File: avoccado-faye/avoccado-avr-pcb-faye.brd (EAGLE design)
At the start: 25 x 24.5 mm, 58 parts, among them Q1 16MHz, Q2 FET, U2 MCP73831

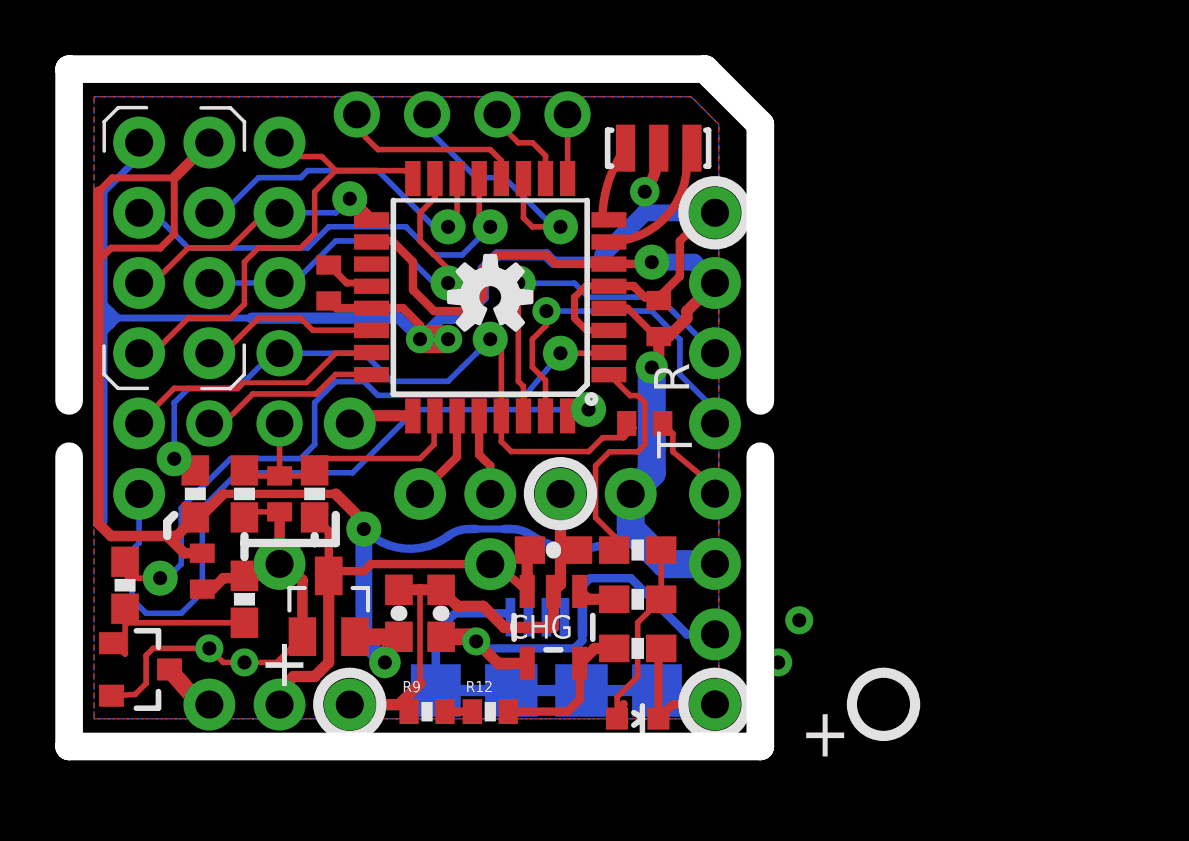
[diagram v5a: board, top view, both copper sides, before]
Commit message: add test points
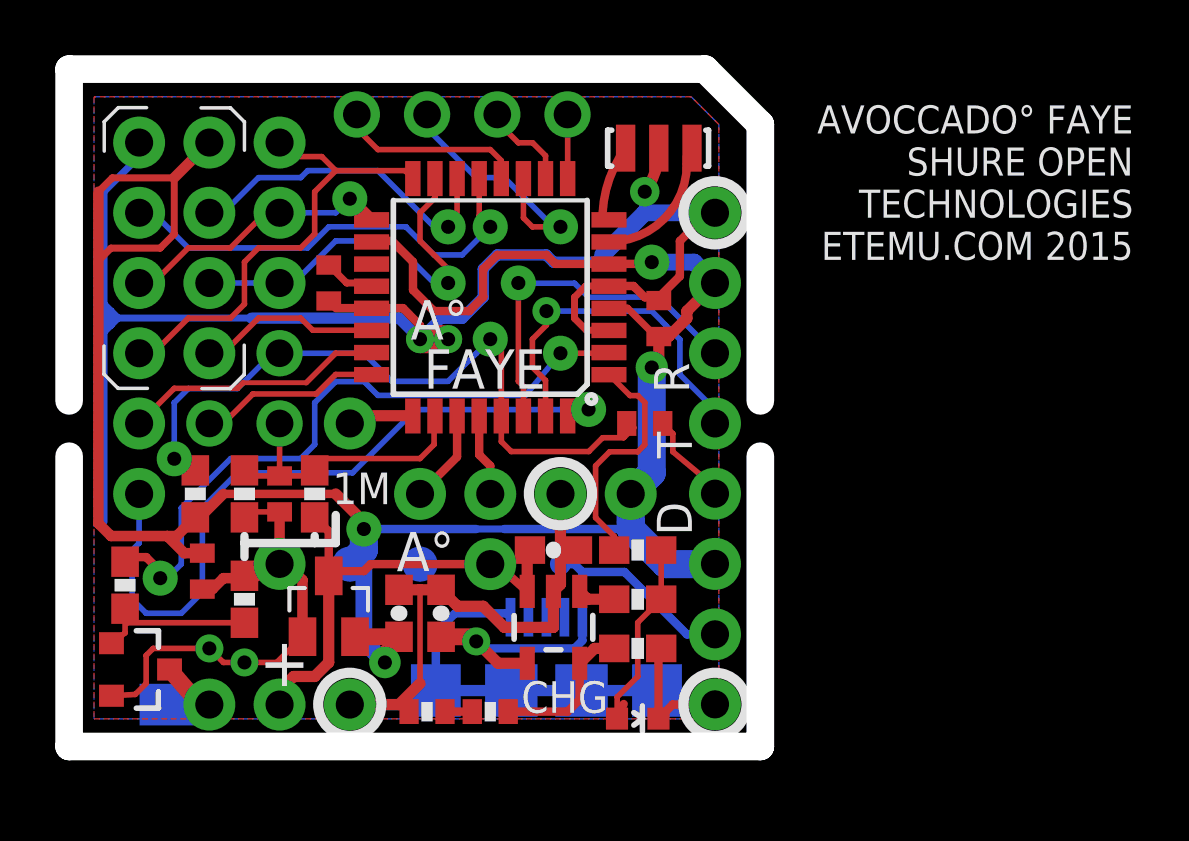
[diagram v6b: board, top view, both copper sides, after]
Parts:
- added JP16: M01SMD-4.5X1.5, SparkFun-Connectors:PAD-1.5X4.5
- added TP3, TP5: TEST-POINT3X5, SparkFun-Passives:PAD.03X.05
- added TP4: TEST-POINT3, SparkFun-Passives:PAD.03X.03
- moved LOGO2 8.27 mm to (20.8, 21.3), flipped to the bottom
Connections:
- net 3.3V: now also TP5.P$1
- net 5V: now also TP4.P$1
- net GND: now also TP3.P$1
- net VIBR: now also JP16.P$1
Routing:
- net VIBR: track 2.02 -> 3.55 mm
- net 3.3V: track 84.7 -> 86.2 mm
- net 5V: track 15.3 -> 16.7 mm
- net N$6: track 6.62 -> 5.85 mm
- net GND: vias 7 -> 5
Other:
- board text added: "1M"
- board text added: "4"
- board text added: "A°"
- board text added: "BAT"
- board text added: "D"
- board text added: "FAYE"
- board text added: "VB"
- board text added: "VC"
- board text removed: "D4"
- board text removed: "DT"
- board text removed: "RX"
- board text removed: "TX"
- board text removed: "Vb"
- board text removed: "Vc"
- board text removed: "Vin"

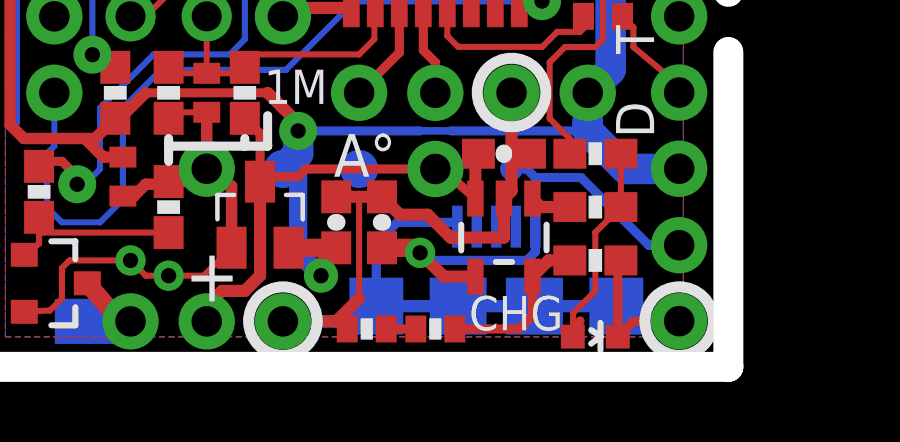
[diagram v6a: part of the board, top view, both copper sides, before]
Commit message: spread 0402 resistors
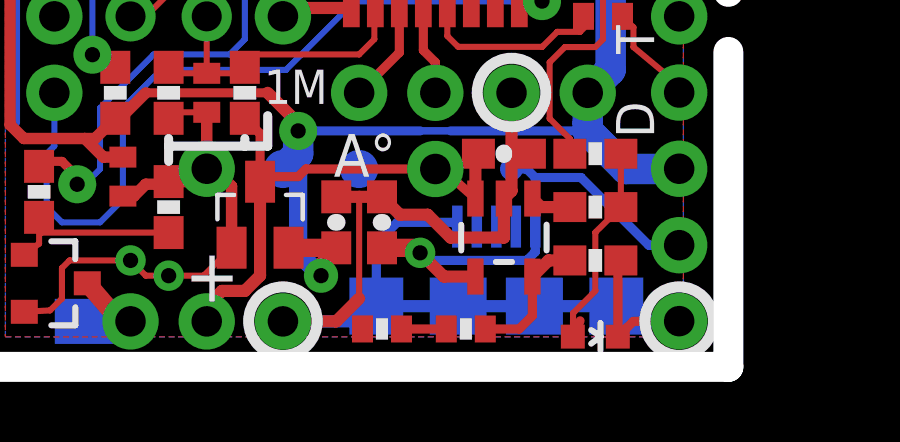
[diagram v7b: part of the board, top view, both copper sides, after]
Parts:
- moved R12 1.02 mm to (15.7, 0.76)
- moved R9 0.51 mm to (13.0, 0.76)
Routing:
- net CHG-PROG: track 5.55 -> 4.53 mm
- net N$3: track 0.99 -> 1.49 mm
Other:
- board text removed: "CHG"
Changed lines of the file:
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@@
 <text x="21.29" y="13.384" size="1.27" layer="21" ratio="15" rot="SR90" align="center-right">R</text>
 <rectangle x1="10.668" y1="11.684" x2="18.796" y2="19.812" layer="41"/>
-<text x="18.996" y="1.289" size="1.143" layer="21" font="vector" ratio="15" rot="R180" align="center-left">CHG</text>
 <circle x="17.272" y="8.644" radius="1.143" width="0.3683" layer="21"/>
 <circle x="22.86" y="1.024" radius="1.143" width="0.3683" layer="21"/>
@@
 <param name="dpMaxLengthDifference" value="10mm"/>
 <param name="dpGapFactor" value="2.5"/>
-<param name="checkGrid" value="1"/>
-<param name="checkAngle" value="1"/>
+<param name="checkGrid" value="0"/>
+<param name="checkAngle" value="0"/>
 <param name="checkFont" value="1"/>
 <param name="checkRestrict" value="0"/>
@@
 <attribute name="PROD_ID" value="CONN-09505" x="16.764" y="1.524" size="1.778" layer="28" font="vector" ratio="15" rot="MR0" display="off"/>
 </element>
-<element name="R12" library="SparkFun-Resistors" package="0402-RES" value="1K" x="14.732" y="0.762" smashed="yes">
-<attribute name="VALUE" x="14.4145" y="1.397" size="0.4064" layer="27"/>
+<element name="R12" library="SparkFun-Resistors" package="0402-RES" value="1K" x="15.748" y="0.762" smashed="yes">
+<attribute name="VALUE" x="15.4305" y="1.397" size="0.4064" layer="27"/>
 </element>
-<element name="R9" library="SparkFun-Resistors" package="0402-RES" value="1K" x="12.446" y="0.762" smashed="yes">
-<attribute name="VALUE" x="12.1285" y="1.397" size="0.4064" layer="27"/>
+<element name="R9" library="SparkFun-Resistors" package="0402-RES" value="1K" x="12.954" y="0.762" smashed="yes">
+<attribute name="VALUE" x="12.6365" y="1.397" size="0.4064" layer="27"/>
 </element>
 <element name="TP5" library="SparkFun-Passives" package="PAD.03X.05" value="TEST-POINT3X5" x="9.652" y="6.096" rot="MR0"/>
@@
 <wire x1="17.968" y1="2.5099" x2="17.968" y2="1.204" width="0.3048" layer="1"/>
 <wire x1="17.968" y1="1.204" x2="17.526" y2="0.762" width="0.3048" layer="1"/>
-<wire x1="17.526" y1="0.762" x2="15.382" y2="0.762" width="0.3048" layer="1"/>
+<wire x1="17.526" y1="0.762" x2="16.398" y2="0.762" width="0.3048" layer="1"/>
 </signal>
 <signal name="5V">
@@
 <contactref element="R12" pad="1"/>
 <contactref element="R9" pad="2"/>
-<wire x1="14.082" y1="0.762" x2="13.096" y2="0.762" width="0.3048" layer="1"/>
+<wire x1="15.098" y1="0.762" x2="13.604" y2="0.762" width="0.3048" layer="1"/>
 </signal>
 </signals>

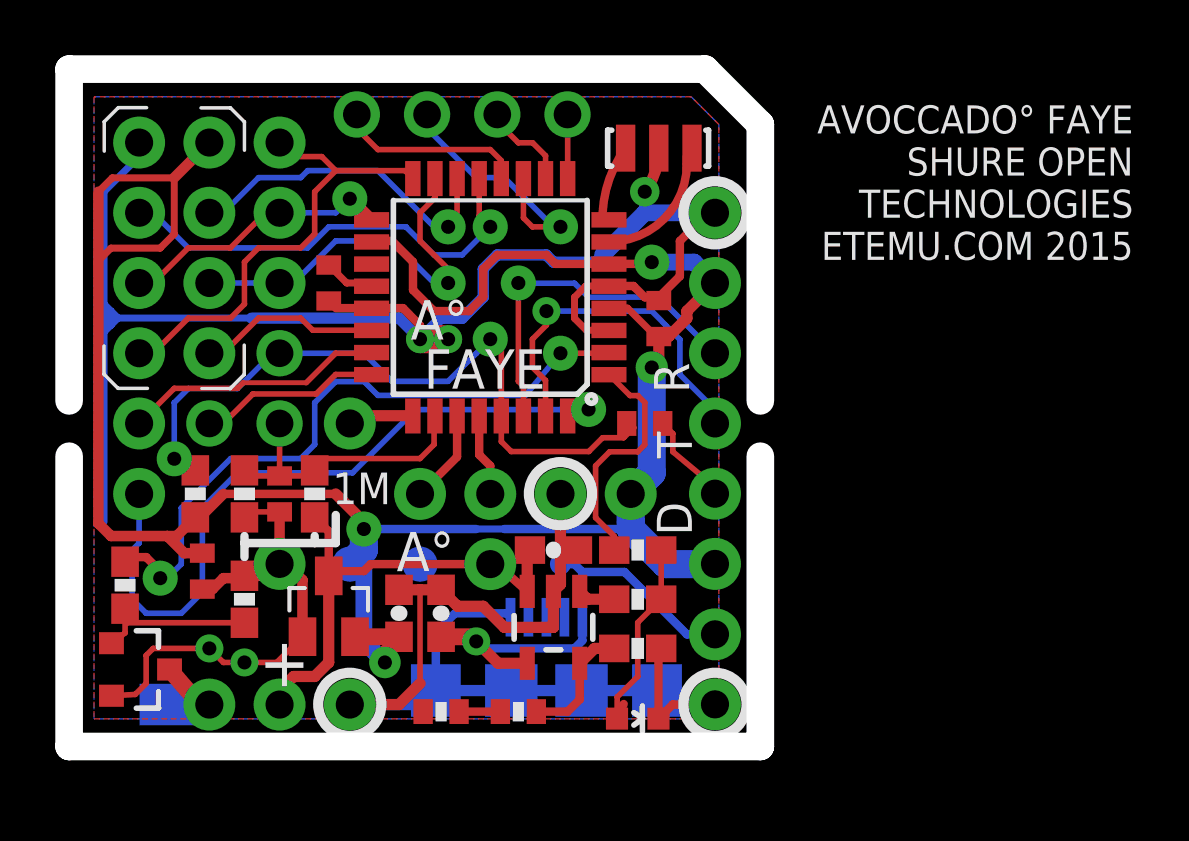
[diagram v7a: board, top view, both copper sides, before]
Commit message: new: all headers on 100mil grid
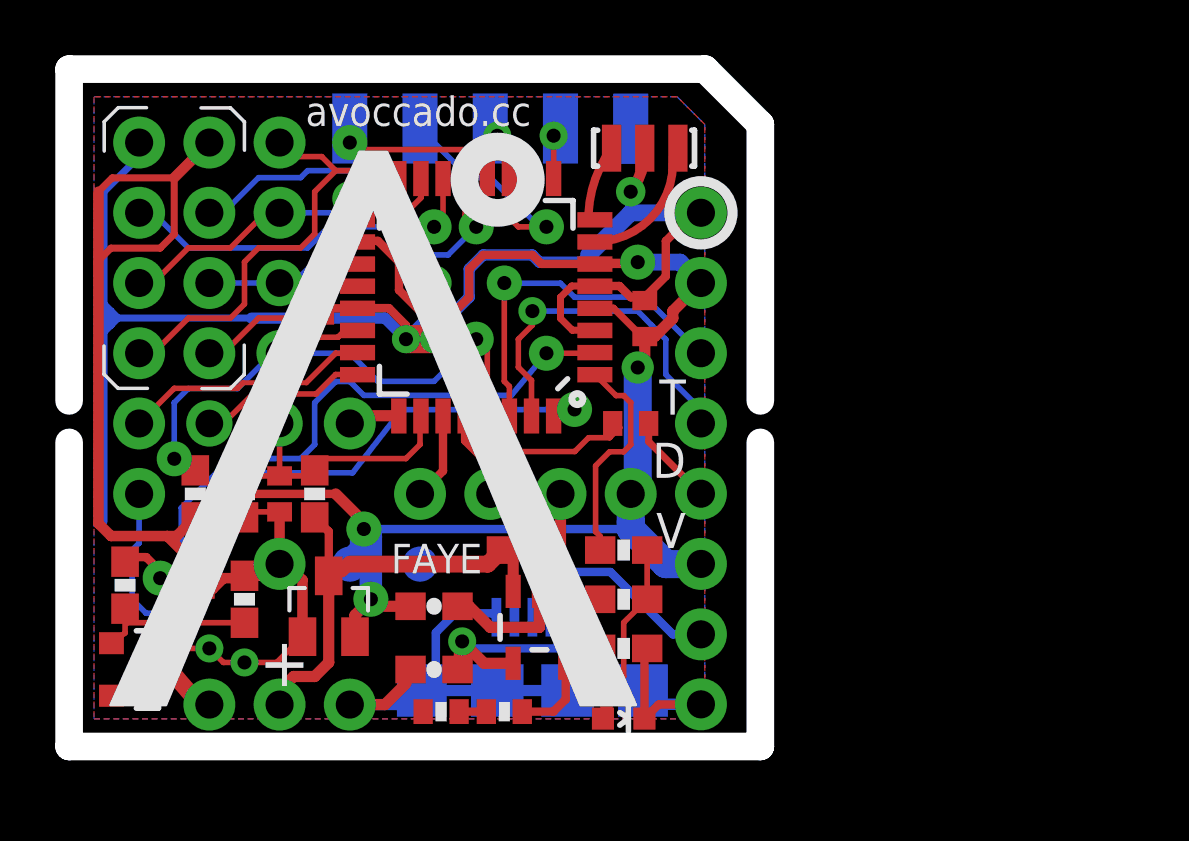
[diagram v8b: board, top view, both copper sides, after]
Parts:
- removed JP1: M01PTH, SparkFun-Connectors:1X01
- removed JP16: M01SMD-4.5X1.5, SparkFun-Connectors:PAD-1.5X4.5
- added TP9: TEST-POINT2, SparkFun-Passives:PAD.02X.02
- JP14: value M01PTH -> M01NOSILK-KIT; device SparkFun-Connectors:1X01 -> SparkFun-Connectors:1X01NS-KIT
- TP1, TP6, TP7, TP8: value M01NOSILK-KIT -> TEST-POINT2; device SparkFun-Connectors:1X01NS-KIT -> SparkFun-Passives:PAD.02X.02
- moved LOGO2 8.65 mm to (14.2, 15.8)
- moved C4 2.05 mm to (12.7, 2.29), turned to 180 degrees
- moved C6 1.30 mm to (12.7, 4.57), turned to 0 degrees
- moved C5 1.02 mm to (16.0, 6.60)
- moved C1 0.57 mm to (8.64, 15.8)
- moved TP1 0.57 mm to (17.3, 21.9), flipped to the bottom
- moved TP6 0.57 mm to (14.7, 21.9), flipped to the bottom
- moved TP8 0.57 mm to (9.65, 21.9), flipped to the bottom
- moved TP7 0.57 mm to (12.2, 21.9), flipped to the bottom
- moved C2 0.51 mm to (19.8, 11.2)
- moved C3 0.51 mm to (20.3, 15.0)
- moved D1 0.51 mm to (19.6, 0.51)
- moved JP10 0.51 mm to (22.4, 8.64)
- moved JP11 0.51 mm to (22.4, 16.3)
- moved JP17 0.51 mm to (22.4, 3.56)
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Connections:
- net D5: now also TP1.P$1; no longer TP1.1
- net D6: now also TP6.P$1; no longer TP6.1
- net D7: now also TP7.P$1; no longer TP7.1
- net D8: now also TP8.P$1; no longer TP8.1
- net GND: now also TP9.P$1
- net VBAT: no longer JP1.1
- net VIBR: no longer JP16.P$1
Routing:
- net GND: track 121.1 -> 112.3 mm
- net VIBR: track 3.55 -> 2.02 mm
- net 3.3V: track 86.2 -> 85.0 mm
- net VBAT: track 17.7 -> 16.9 mm
- net D7: track 9.71 -> 8.95 mm
- net D3: track 9.15 -> 8.43 mm
- net D6: track 3.34 -> 2.72 mm, vias 0 -> 1
- net 5V: track 16.7 -> 16.1 mm
- net AREF: track 1.98 -> 1.40 mm
- net D8: track 6.86 -> 6.35 mm, vias 0 -> 1
- net MISO: track 17.5 -> 17.0 mm
- net N$3: track 1.49 -> 0.99 mm
- net D10: track 12.0 -> 11.5 mm
- net A3: track 10.9 -> 10.4 mm
- net D9: track 16.3 -> 15.8 mm
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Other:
- outline, holes or cut-outs redrawn
- board text added: "A1"
- board text added: "A3"
- board text added: "D4"
- board text added: "G"
- board text added: "V"
- board text added: "avoccado.cc"
- board text removed: "1M"
- board text removed: "4"
- board text removed: "AVOCCADO° FAYE SHURE OPEN TECHNOLOGIES ETEMU.COM 2015"
- board text removed: "A°"
- board text removed: "VB"
